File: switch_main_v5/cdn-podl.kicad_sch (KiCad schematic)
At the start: 0 parts

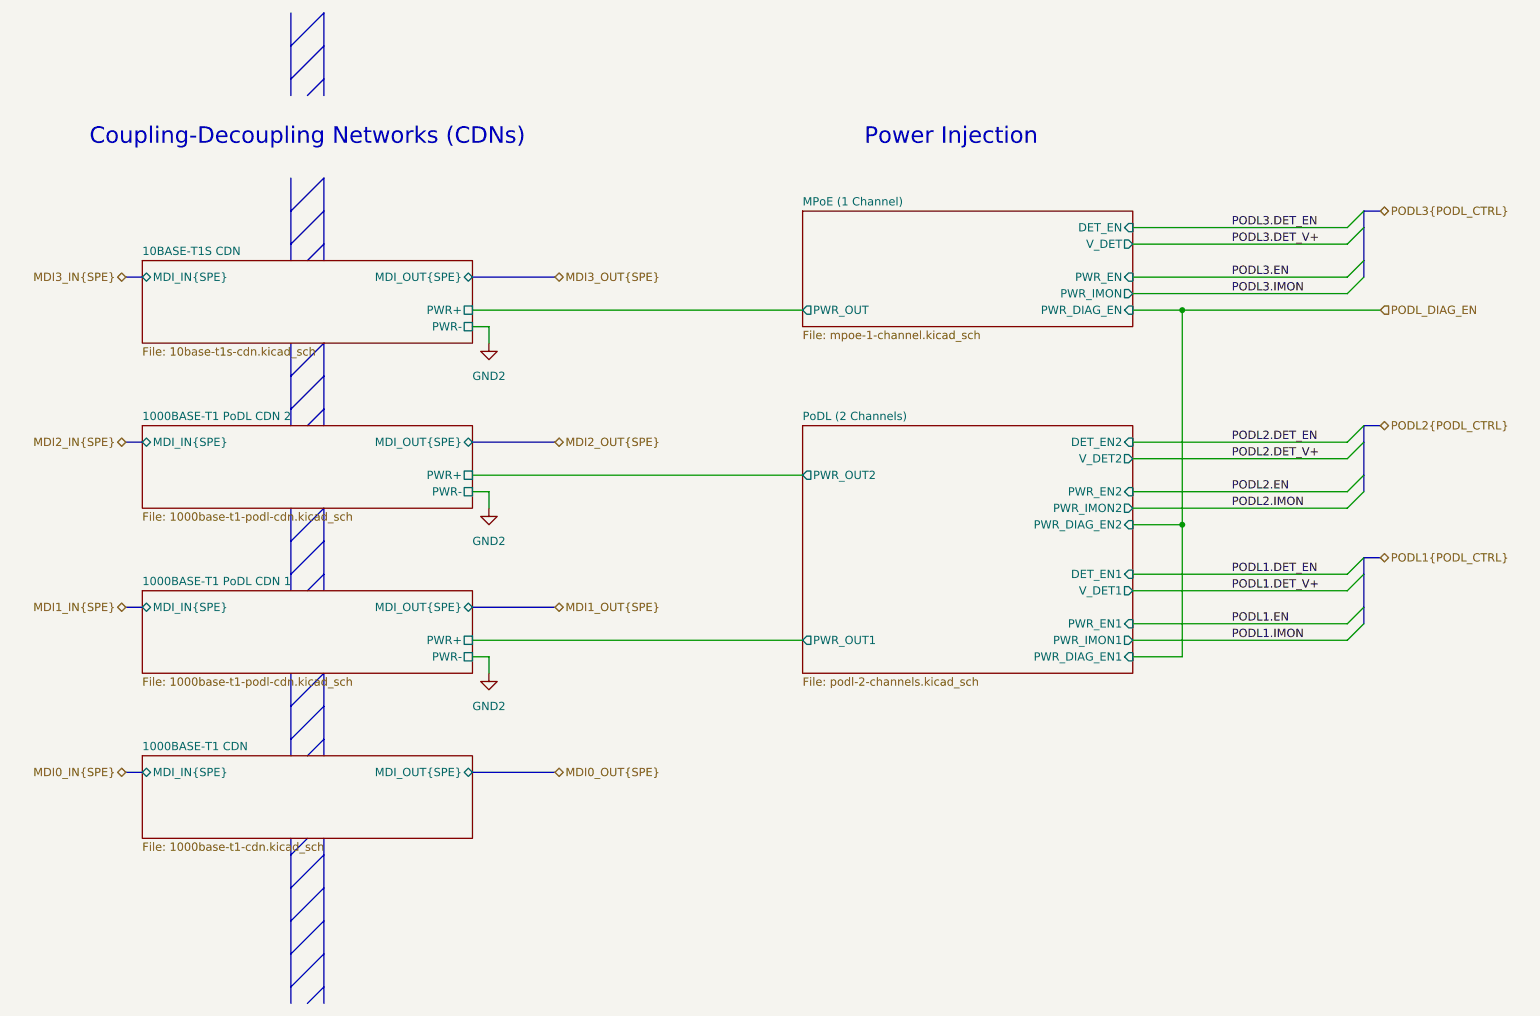
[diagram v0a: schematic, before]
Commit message: MDIO multiplexing
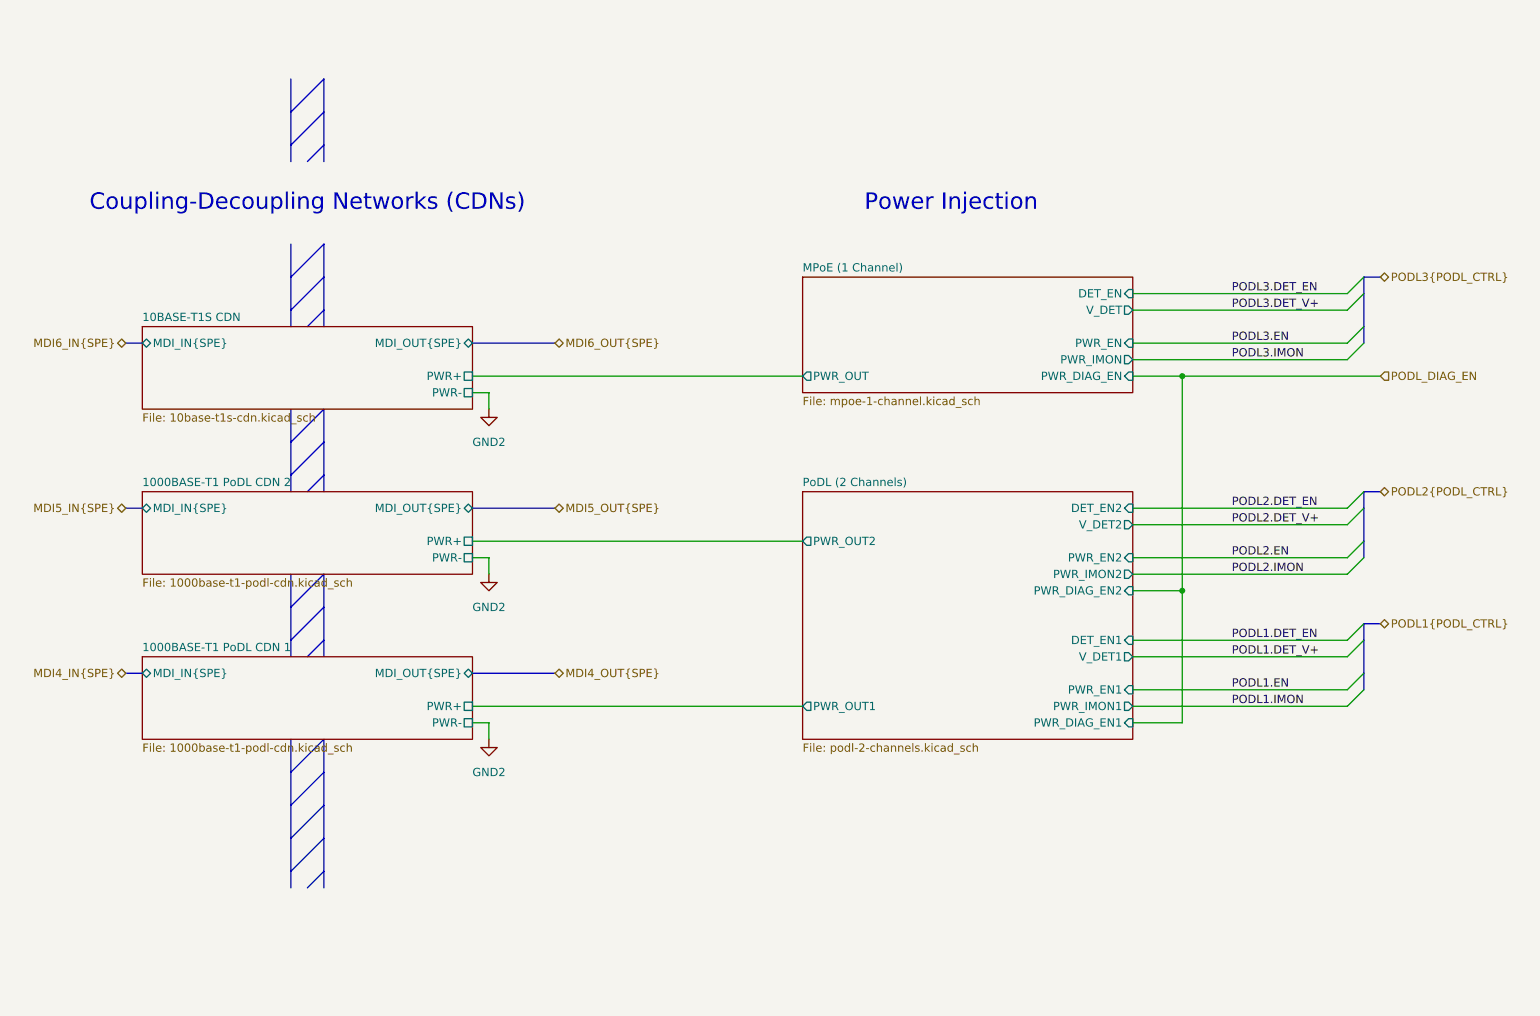
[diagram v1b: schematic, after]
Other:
- removed sheet 1000BASE-T1 CDN
